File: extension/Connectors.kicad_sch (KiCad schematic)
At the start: 2 parts, among them X701 MB2, X702 MB1

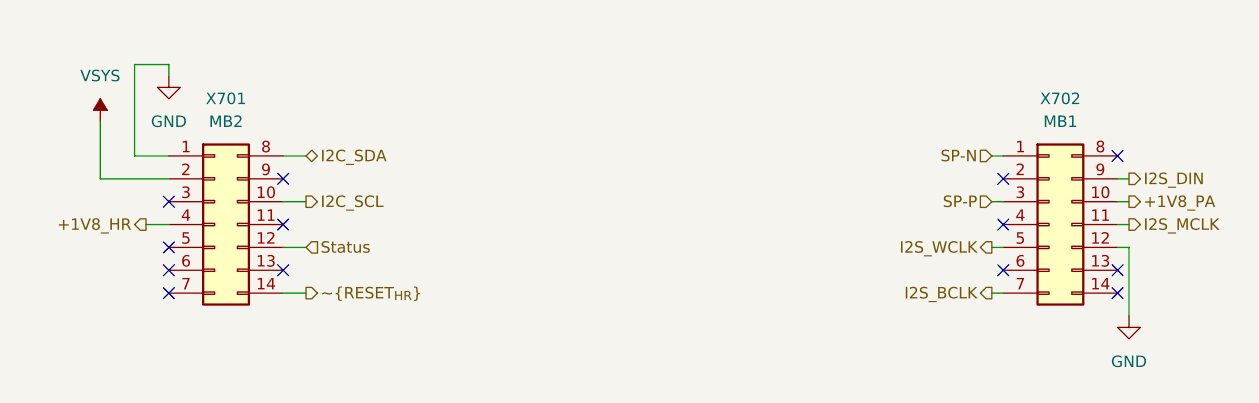
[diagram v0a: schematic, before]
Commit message: Smaller changes for better integration into ZSWatch mainboard
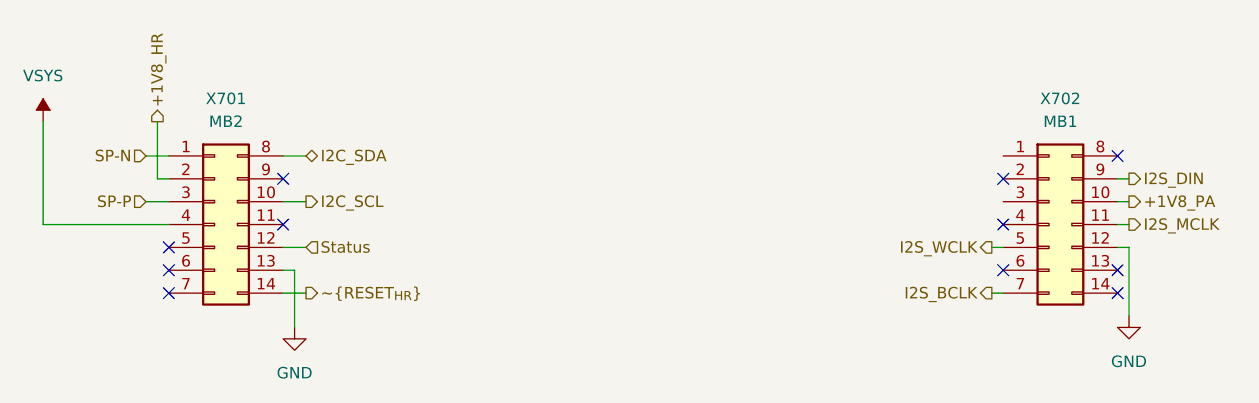
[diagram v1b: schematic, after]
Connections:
- net +1V8_HR: now also X701.2 (Pin_2); no longer X701.4 (Pin_4)
- net GND: now also X701.13 (Pin_13); no longer X701.1 (Pin_1)
- net SP-N: now also X701.1 (Pin_1); no longer X702.1 (Pin_1)
- net SP-P: now also X701.3 (Pin_3); no longer X702.3 (Pin_3)
- net VSYS: now also X701.4 (Pin_4); no longer X701.2 (Pin_2)
- no-connect marks 13 -> 11
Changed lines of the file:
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@@
-	)
-	(no_connect
-		(at 102.87 93.98)
 	)
 	(no_connect
@@
 	)
 	(no_connect
-		(at 115.57 101.6)
-	)
-	(no_connect
 		(at 208.28 88.9)
 	)
@@
 	(wire
 		(pts
-			(xy 99.06 88.9) (xy 99.06 78.74)
-		)
-		(stroke
-			(width 0)
-			(type default)
-		)
-	)
-	(wire
-		(pts
-			(xy 100.33 96.52) (xy 102.87 96.52)
-		)
-		(stroke
-			(width 0)
-			(type default)
-		)
-	)
-	(wire
-		(pts
-			(xy 102.87 88.9) (xy 99.06 88.9)
+			(xy 88.9 96.52) (xy 102.87 96.52)
 		)
 		(stroke
@@
 	(wire
 		(pts
-			(xy 95.25 85.09) (xy 95.25 91.44)
-		)
-		(stroke
-			(width 0)
-			(type default)
-		)
-	)
-	(wire
-		(pts
-			(xy 194.31 88.9) (xy 195.58 88.9)
+			(xy 101.6 85.09) (xy 101.6 91.44)
 		)
 		(stroke
@@
 	(wire
 		(pts
-			(xy 102.87 91.44) (xy 95.25 91.44)
+			(xy 101.6 91.44) (xy 102.87 91.44)
 		)
 		(stroke
@@
 	(wire
 		(pts
-			(xy 102.87 78.74) (xy 102.87 80.01)
-		)
-		(stroke
-			(width 0)
-			(type default)
-		)
-	)
-	(wire
-		(pts
 			(xy 208.28 96.52) (xy 209.55 96.52)
 		)
@@
 	(wire
 		(pts
+			(xy 100.33 88.9) (xy 102.87 88.9)
+		)
+		(stroke
+			(width 0)
+			(type default)
+		)
+	)
+	(wire
+		(pts
 			(xy 208.28 99.06) (xy 209.55 99.06)
 		)
@@
 	(wire
 		(pts
+			(xy 100.33 93.98) (xy 102.87 93.98)
+		)
+		(stroke
+			(width 0)
+			(type default)
+		)
+	)
+	(wire
+		(pts
 			(xy 208.28 91.44) (xy 209.55 91.44)
 		)
@@
 	(wire
 		(pts
+			(xy 88.9 85.09) (xy 88.9 96.52)
+		)
+		(stroke
+			(width 0)
+			(type default)
+		)
+	)
+	(wire
+		(pts
 			(xy 115.57 88.9) (xy 118.11 88.9)
 		)
@@
 	(wire
 		(pts
-			(xy 99.06 78.74) (xy 102.87 78.74)
-		)
-		(stroke
-			(width 0)
-			(type default)
-		)
-	)
-	(wire
-		(pts
-			(xy 194.31 93.98) (xy 195.58 93.98)
+			(xy 116.84 101.6) (xy 116.84 107.95)
 		)
 		(stroke
@@
 		(pts
 			(xy 115.57 93.98) (xy 118.11 93.98)
+		)
+		(stroke
+			(width 0)
+			(type default)
+		)
+	)
+	(wire
+		(pts
+			(xy 115.57 101.6) (xy 116.84 101.6)
 		)
 		(stroke
@@
 	(hierarchical_label "+1V8_HR"
 		(shape output)
-		(at 100.33 96.52 180)
-		(effects
-			(font
-				(size 1.27 1.27)
-			)
-			(justify right)
+		(at 101.6 85.09 90)
+		(effects
+			(font
+				(size 1.27 1.27)
+			)
+			(justify left)
 		)
 	)
 	(hierarchical_label "SP-N"
 		(shape input)
-		(at 194.31 88.9 180)
+		(at 100.33 88.9 180)
 		(effects
 			(font
@@
 	(hierarchical_label "SP-P"
 		(shape input)
-		(at 194.31 93.98 180)
+		(at 100.33 93.98 180)
 		(effects
 			(font
@@
 	)
 	(symbol
+		(lib_id "power:GND")
+		(at 116.84 107.95 0)
+		(unit 1)
+		(exclude_from_sim no)
+		(in_bom yes)
+		(on_board yes)
+		(dnp no)
+		(fields_autoplaced yes)
+		(property "Reference" "#PWR0703"
+			(at 116.84 114.3 0)
+			(effects
+				(font
+					(size 1.27 1.27)
+				)
+				(hide yes)
+			)
+		)
+		(property "Value" "GND"
+			(at 116.84 113.03 0)
+			(effects
+				(font
+					(size 1.27 1.27)
+				)
+			)
+		)
+		(property "Footprint" ""
+			(at 116.84 107.95 0)
+			(effects
+				(font
+					(size 1.27 1.27)
+				)
+				(hide yes)
+			)
+		)
+		(property "Datasheet" ""
+			(at 116.84 107.95 0)
+			(effects
+				(font
+					(size 1.27 1.27)
+				)
+				(hide yes)
+			)
+		)
+		(property "Description" "Power symbol creates a global label with name \"GND\" , ground"
+			(at 116.84 107.95 0)
+			(effects
+				(font
+					(size 1.27 1.27)
+				)
+				(hide yes)
+			)
+		)
+		(pin "1"
+		)
+		(instances
+			(project "ZSWatch-Extension"
+				(path "/d5742f03-3b1a-42e5-a384-018bd4b919aa/c5103ceb-5325-4a84-a025-9638a412984e/84d69b6e-c5e1-430b-bee6-3e9322ea9cdc"
+					(reference "#PWR0703")
+					(unit 1)
+				)
+			)
+		)
+	)
+	(symbol
 		(lib_id "power:VS")
-		(at 95.25 85.09 0)
+		(at 88.9 85.09 0)
 		(unit 1)
 		(exclude_from_sim no)
@@
 		(fields_autoplaced yes)
 		(property "Reference" "#PWR0701"
-			(at 95.25 88.9 0)
+			(at 88.9 88.9 0)
 			(effects
 				(font
@@
 		)
 		(property "Value" "VSYS"
-			(at 95.25 80.01 0)
+			(at 88.9 80.01 0)
 			(effects
 				(font
@@
 		)
 		(property "Footprint" ""
-			(at 95.25 85.09 0)
+			(at 88.9 85.09 0)
 			(effects
 				(font
@@
 		)
 		(property "Datasheet" ""
-			(at 95.25 85.09 0)
+			(at 88.9 85.09 0)
 			(effects
 				(font
@@
 		)
 		(property "Description" "Power symbol creates a global label with name \"VS\""
-			(at 95.25 85.09 0)
+			(at 88.9 85.09 0)
 			(effects
 				(font
@@
 		)
 		(property "manf" ""
-			(at 95.25 85.09 0)
+			(at 88.9 85.09 0)
 			(effects
 				(font
@@
 		)
 		(property "manf#" ""
-			(at 95.25 85.09 0)
+			(at 88.9 85.09 0)
 			(effects
 				(font
@@
 		)
 		(property "mouser#" ""
-			(at 95.25 85.09 0)
+			(at 88.9 85.09 0)
 			(effects
 				(font
@@
 		)
 		(property "CONFIG" ""
-			(at 95.25 85.09 0)
+			(at 88.9 85.09 0)
 			(effects
 				(font
@@
 					(unit 1)
 				)
-			)
-		)
-	)
-	(symbol
-		(lib_id "power:GND")
-		(at 102.87 80.01 0)
-		(unit 1)
-		(exclude_from_sim no)
-		(in_bom yes)
-		(on_board yes)
-		(dnp no)
-		(fields_autoplaced yes)
-		(property "Reference" "#PWR0702"
-			(at 102.87 86.36 0)
-			(effects
-				(font
-					(size 1.27 1.27)
-				)
-				(hide yes)
-			)
-		)
-		(property "Value" "GND"
-			(at 102.87 85.09 0)
-			(effects
-				(font
-					(size 1.27 1.27)
-				)
-			)
-		)
-		(property "Footprint" ""
-			(at 102.87 80.01 0)
-			(effects
-				(font
-					(size 1.27 1.27)
-				)
-				(hide yes)
-			)
-		)
-		(property "Datasheet" ""
-			(at 102.87 80.01 0)
-			(effects
-				(font
-					(size 1.27 1.27)
-				)
-				(hide yes)
-			)
-		)
-		(property "Description" "Power symbol creates a global label with name \"GND\" , ground"
-			(at 102.87 80.01 0)
-			(effects
-				(font
-					(size 1.27 1.27)
-				)
-				(hide yes)
-			)
-		)
-		(pin "1"
-		)
-		(instances
-			(project "ZSWatch-Extension"
-				(path "/d5742f03-3b1a-42e5-a384-018bd4b919aa/c5103ceb-5325-4a84-a025-9638a412984e/84d69b6e-c5e1-430b-bee6-3e9322ea9cdc"
-					(reference "#PWR0702")
-					(unit 1)
-				)

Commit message: Change connector layout to simplify routing on the watch PCB
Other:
- title: Heartrate-DevKit -> Connectors
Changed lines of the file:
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@@
 	(paper "A4")
 	(title_block
-		(title "Heartrate-DevKit")
+		(title "Connectors")
 		(date "2025-07-13")
 		(rev "${REVISION}")
